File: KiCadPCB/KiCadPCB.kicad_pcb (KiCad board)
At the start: 2 copper layers, 152.4 x 48.9 mm, 31 parts, among them SW1 M1, SW10 M10, SW11 M11, SW12 M12, SW13 M13, SW14 ENCODER, SW2 M2, SW3 M3, SW4 M4, SW5 M5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

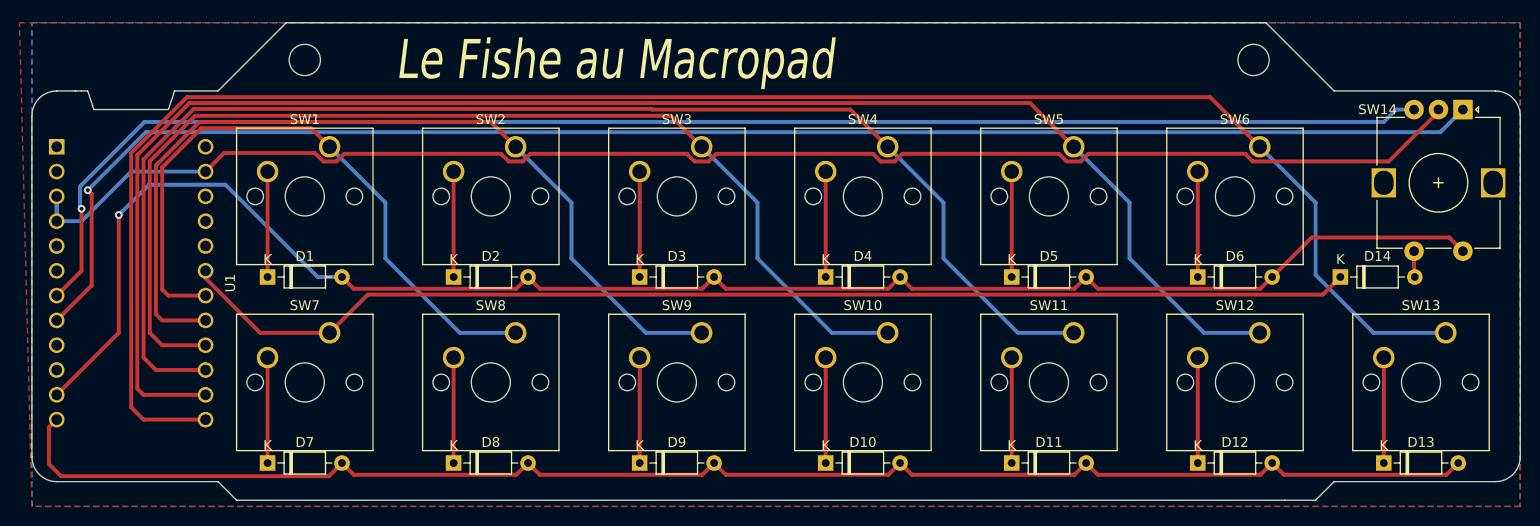
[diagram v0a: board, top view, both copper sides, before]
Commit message: Updated the PCB files to have supports in the top right section - pressing the encoder causes the macropad to tip over.
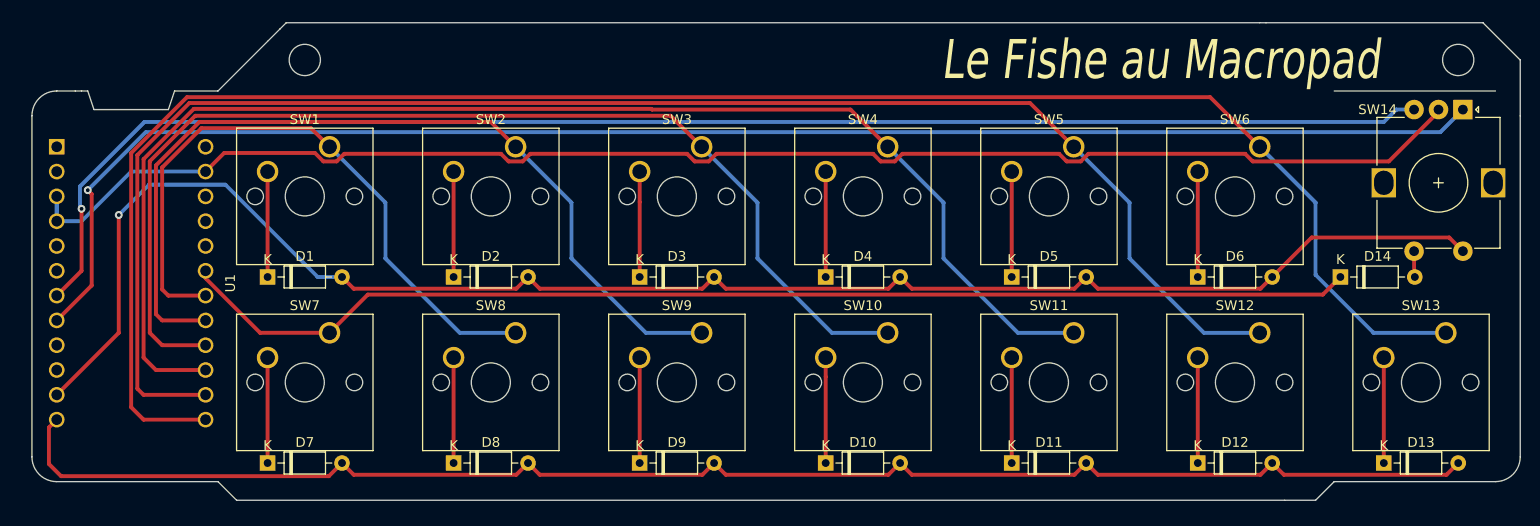
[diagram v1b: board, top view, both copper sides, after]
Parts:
- moved H2 21.0 mm to (223.5, 27.9)
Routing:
- removed copper zone on B.Cu, net (none)
- removed copper zone on F.Cu, net GND
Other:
- outline, holes or cut-outs redrawn
- net class Default removed

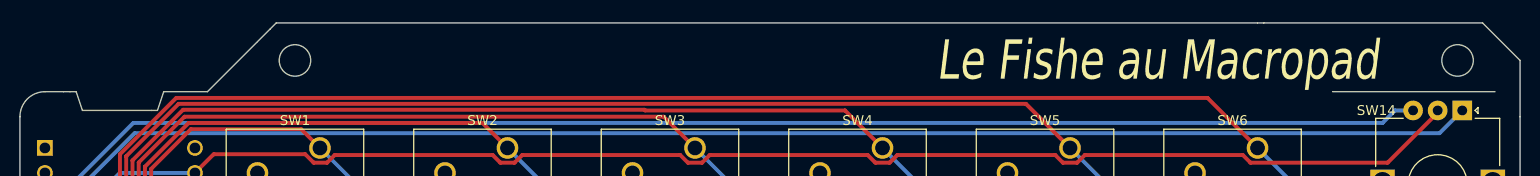
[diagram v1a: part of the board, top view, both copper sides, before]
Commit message: Removed the edge cuts where the USB connector is on the promicro.
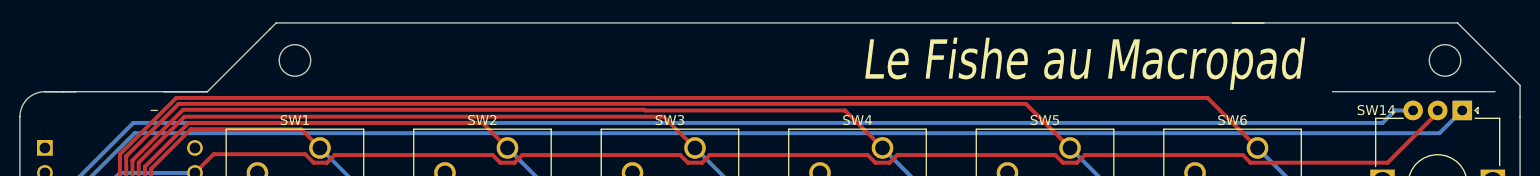
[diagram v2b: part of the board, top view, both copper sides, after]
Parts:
- moved H2 1.27 mm to (222.2, 27.9)
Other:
- outline, holes or cut-outs redrawn
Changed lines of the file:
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@@
   )
   (footprint "MountingHole:MountingHole_3.2mm_M3" (layer "F.Cu")
-    (at 223.52 27.94)
+    (at 222.25 27.94)
     (descr "Mounting Hole 3.2mm, no annular, M3")
     (tags "mounting hole 3.2mm no annular m3")
@@
   (gr_line (start 229.87 33.655) (end 229.87 68.58) (layer "Edge.Cuts") (width 0.05))
   (gr_line (start 210.82 71.12) (end 227.33 71.12) (layer "Edge.Cuts") (width 0.05))
-  (gr_line (start 83.82 33.02) (end 90.805 33.02) (layer "Edge.Cuts") (width 0.05))
   (gr_line (start 81.915 31.115) (end 80.01 31.115) (layer "Edge.Cuts") (width 0.05))
   (gr_line (start 82.55 31.115) (end 81.915 31.115) (layer "Edge.Cuts") (width 0.05))
@@
   (gr_line (start 203.835 24.13) (end 203.2 24.13) (layer "Edge.Cuts") (width 0.05))
   (gr_line (start 102.87 24.765) (end 103.505 24.13) (layer "Edge.Cuts") (width 0.05))
-  (gr_line (start 91.44 33.02) (end 92.075 31.115) (layer "Edge.Cuts") (width 0.05))
   (gr_line (start 96.52 31.115) (end 101.6 26.035) (layer "Edge.Cuts") (width 0.05))
-  (gr_line (start 229.87 27.94) (end 229.87 33.655) (layer "Edge.Cuts") (width 0.05))
-  (gr_line (start 83.82 33.02) (end 83.185 31.115) (layer "Edge.Cuts") (width 0.05))
-  (gr_line (start 203.835 24.13) (end 226.06 24.13) (layer "Edge.Cuts") (width 0.05))
   (gr_line (start 96.52 71.12) (end 98.425 73.025) (layer "Edge.Cuts") (width 0.05))
+  (gr_line (start 80.01 31.115) (end 96.52 31.115) (layer "Edge.Cuts") (width 0.05))
   (gr_line (start 101.6 26.035) (end 102.87 24.765) (layer "Edge.Cuts") (width 0.05))
+  (gr_line (start 223.52 24.13) (end 200.66 24.13) (layer "Edge.Cuts") (width 0.05))
   (gr_arc (start 229.87 68.58) (mid 229.126051 70.376051) (end 227.33 71.12) (layer "Edge.Cuts") (width 0.05))
   (gr_line (start 103.505 24.13) (end 203.2 24.13) (layer "Edge.Cuts") (width 0.05))
@@
   (gr_line (start 205.74 73.025) (end 208.915 73.025) (layer "Edge.Cuts") (width 0.05))
   (gr_arc (start 80.01 71.12) (mid 78.213949 70.376051) (end 77.47 68.58) (layer "Edge.Cuts") (width 0.05))
+  (gr_line (start 229.87 33.655) (end 229.87 30.48) (layer "Edge.Cuts") (width 0.05))
   (gr_line (start 90.805 33.02) (end 91.44 33.02) (layer "Edge.Cuts") (width 0.05))
   (gr_line (start 80.01 71.12) (end 96.52 71.12) (layer "Edge.Cuts") (width 0.05))
-  (gr_line (start 226.06 24.13) (end 229.87 27.94) (layer "Edge.Cuts") (width 0.05))
+  (gr_line (start 229.87 30.48) (end 223.52 24.13) (layer "Edge.Cuts") (width 0.05))
   (gr_text "JLCJLCJLCJLC" (at 191.77 72.39) (layer "B.SilkS")
     (effects (font (size 1 1) (thickness 0.15)) (justify mirror))
   )
-  (gr_text "Le Fishe au Macropad" (at 193.04 27.94) (layer "F.SilkS")
+  (gr_text "Le Fishe au Macropad" (at 185.42 27.94) (layer "F.SilkS")
     (effects (font (size 4 3) (thickness 0.5) italic))
   )
